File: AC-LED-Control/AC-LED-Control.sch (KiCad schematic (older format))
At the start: 20 parts, among them P101 CONN_01X02, P102 CONN_01X02, P103 CONN_01X04, SW101 SW_PUSH, U101 FOD814-D, U102 STM32F030F4P6, U103 74HC595, U104 74HC595

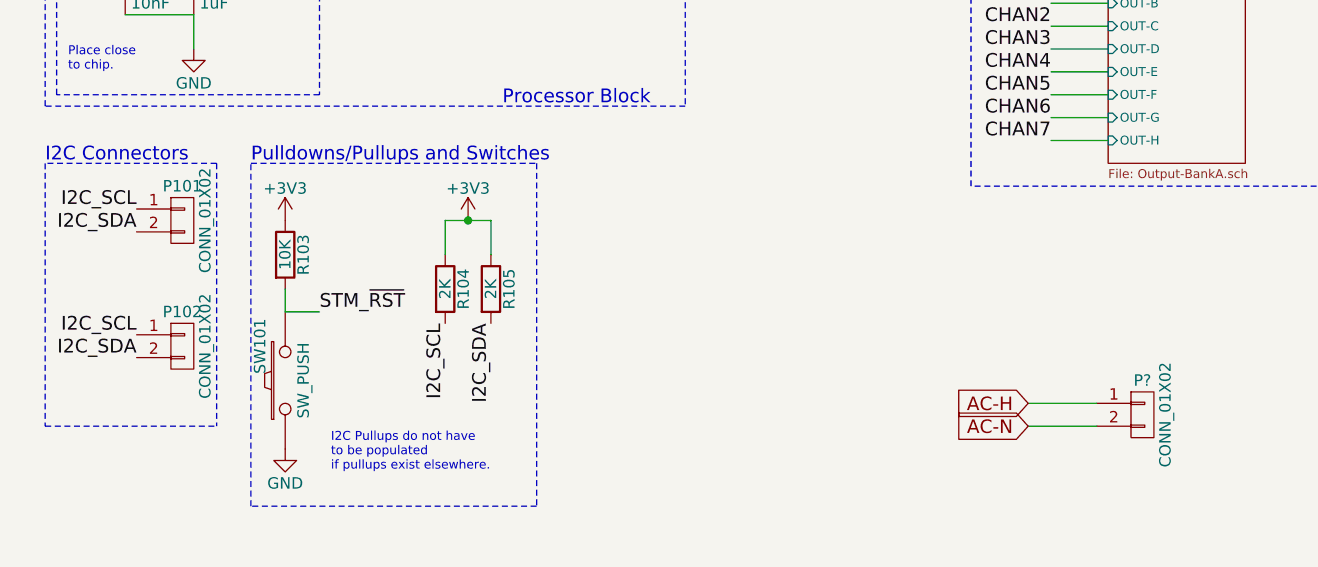
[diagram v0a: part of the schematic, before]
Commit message: Associated footprints
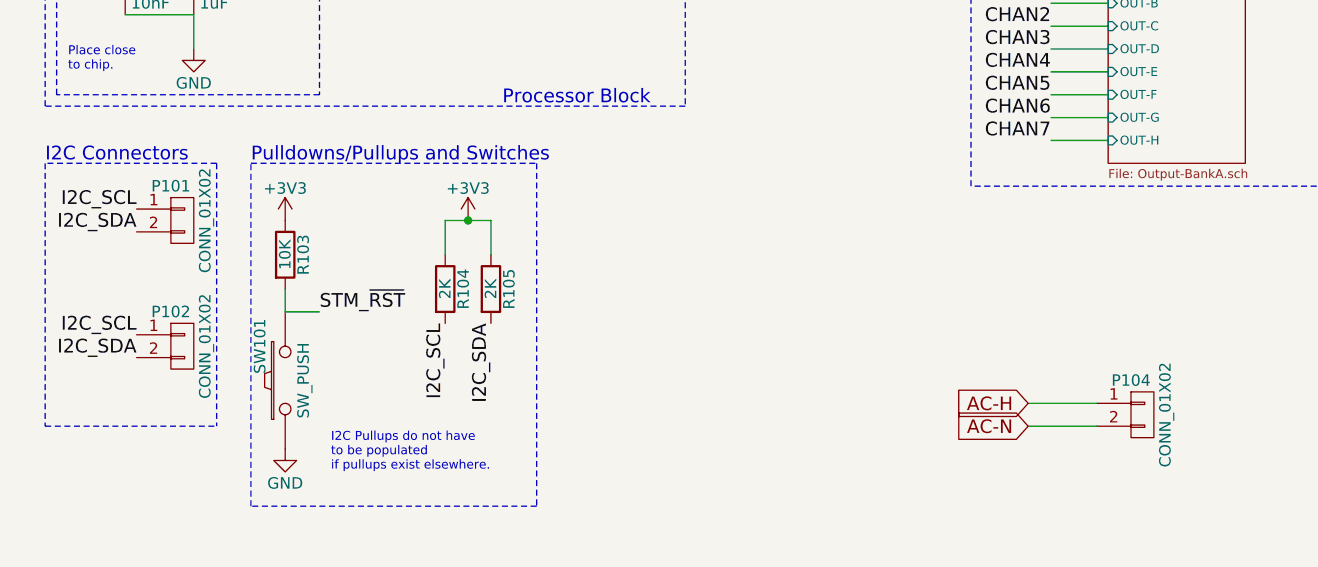
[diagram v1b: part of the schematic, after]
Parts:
- C101, C102, C103, C104, C105: footprint (none) -> Capacitors_SMD:C_0603_HandSoldering
- P101, P102: footprint (none) -> Pin_Headers:Pin_Header_Straight_1x02
- P103: footprint (none) -> Pin_Headers:Pin_Header_Straight_1x04
- R101, R102, R103, R104, R105, R106: footprint (none) -> Resistors_SMD:R_0603_HandSoldering
- SW101: footprint (none) -> Buttons_Switches_SMD:SW_SPST_EVPBF
- U101: footprint (none) -> onsemi:OnSemi_PDIP4
- U102: footprint (none) -> Housings_SSOP:TSSOP-20_4.4x6.5mm_Pitch0.65mm
- U103, U104: footprint (none) -> Housings_SOIC:SOIC-16_3.9x9.9mm_Pitch1.27mm
- gave numbers to parts that had none: 1
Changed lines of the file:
@@
 F 0 "U102" H 2200 700 60  0000 C CNN
 F 1 "STM32F030F4P6" H 2200 1950 60  0000 C CNN
-F 2 "" H 2150 1400 60  0000 C CNN
+F 2 "Housings_SSOP:TSSOP-20_4.4x6.5mm_Pitch0.65mm" H 2150 1400 60  0001 C CNN
 F 3 "" H 2150 1400 60  0000 C CNN
 	1    2200 1400
@@
 U 1 1 5B453C99
 P 1300 4350
-F 0 "P101" H 1300 4500 50  0000 C CNN
+F 0 "P101" H 1250 4500 50  0000 C CNN
 F 1 "CONN_01X02" V 1400 4350 50  0000 C CNN
-F 2 "" H 1300 4350 50  0000 C CNN
+F 2 "Pin_Headers:Pin_Header_Straight_1x02" H 1300 4350 50  0001 C CNN
 F 3 "" H 1300 4350 50  0000 C CNN
 	1    1300 4350
@@
 U 1 1 5B453DC6
 P 1300 4900
-F 0 "P102" H 1300 5050 50  0000 C CNN
+F 0 "P102" H 1250 5050 50  0000 C CNN
 F 1 "CONN_01X02" V 1400 4900 50  0000 C CNN
-F 2 "" H 1300 4900 50  0000 C CNN
+F 2 "Pin_Headers:Pin_Header_Straight_1x02" H 1300 4900 50  0001 C CNN
 F 3 "" H 1300 4900 50  0000 C CNN
 	1    1300 4900
@@
 F 0 "R104" V 2530 4650 50  0000 C CNN
 F 1 "2K" V 2450 4650 50  0000 C CNN
-F 2 "" V 2380 4650 50  0000 C CNN
+F 2 "Resistors_SMD:R_0603_HandSoldering" V 2380 4650 50  0001 C CNN
 F 3 "" H 2450 4650 50  0000 C CNN
 	1    2450 4650
@@
 F 0 "R105" V 2730 4650 50  0000 C CNN
 F 1 "2K" V 2650 4650 50  0000 C CNN
-F 2 "" V 2580 4650 50  0000 C CNN
+F 2 "Resistors_SMD:R_0603_HandSoldering" V 2580 4650 50  0001 C CNN
 F 3 "" H 2650 4650 50  0000 C CNN
 	1    2650 4650
@@
 $EndComp
 $Comp
-L +3V3 #PWR108
+L +3V3 #PWR01
 U 1 1 5B45401C
 P 2550 4350
-F 0 "#PWR108" H 2550 4200 50  0001 C CNN
+F 0 "#PWR01" H 2550 4200 50  0001 C CNN
 F 1 "+3V3" H 2550 4490 50  0000 C CNN
 F 2 "" H 2550 4350 50  0000 C CNN
@@
 F 0 "C101" H 1075 2750 50  0000 L CNN
 F 1 "100nF" H 1075 2550 50  0000 L CNN
-F 2 "" H 1088 2500 50  0000 C CNN
+F 2 "Capacitors_SMD:C_0603_HandSoldering" H 1088 2500 50  0001 C CNN
 F 3 "" H 1050 2650 50  0000 C CNN
 	1    1050 2650
@@
 F 0 "C103" H 1375 2750 50  0000 L CNN
 F 1 "100nF" H 1375 2550 50  0000 L CNN
-F 2 "" H 1388 2500 50  0000 C CNN
+F 2 "Capacitors_SMD:C_0603_HandSoldering" H 1388 2500 50  0001 C CNN
 F 3 "" H 1350 2650 50  0000 C CNN
 	1    1350 2650
@@
 F 0 "C105" H 1675 2750 50  0000 L CNN
 F 1 "4.7uF" H 1675 2550 50  0000 L CNN
-F 2 "" H 1688 2500 50  0000 C CNN
+F 2 "Capacitors_SMD:C_0603_HandSoldering" H 1688 2500 50  0001 C CNN
 F 3 "" H 1650 2650 50  0000 C CNN
 	1    1650 2650
@@
 	1400 1750 1400 1850
 $Comp
-L GND #PWR104
+L GND #PWR02
 U 1 1 5B454DB5
 P 1400 1850
-F 0 "#PWR104" H 1400 1600 50  0001 C CNN
+F 0 "#PWR02" H 1400 1600 50  0001 C CNN
 F 1 "GND" H 1400 1700 50  0000 C CNN
 F 2 "" H 1400 1850 50  0000 C CNN
@@
 $EndComp
 $Comp
-L GND #PWR105
+L GND #PWR03
 U 1 1 5B454DF7
 P 1650 2900
-F 0 "#PWR105" H 1650 2650 50  0001 C CNN
+F 0 "#PWR03" H 1650 2650 50  0001 C CNN
 F 1 "GND" H 1650 2750 50  0000 C CNN
 F 2 "" H 1650 2900 50  0000 C CNN
@@
 F 0 "C102" H 1075 3400 50  0000 L CNN
 F 1 "10nF" H 1075 3200 50  0000 L CNN
-F 2 "" H 1088 3150 50  0000 C CNN
+F 2 "Capacitors_SMD:C_0603_HandSoldering" H 1088 3150 50  0001 C CNN
 F 3 "" H 1050 3300 50  0000 C CNN
 	1    1050 3300
@@
 F 0 "C104" H 1375 3400 50  0000 L CNN
 F 1 "1uF" H 1375 3200 50  0000 L CNN
-F 2 "" H 1388 3150 50  0000 C CNN
+F 2 "Capacitors_SMD:C_0603_HandSoldering" H 1388 3150 50  0001 C CNN
 F 3 "" H 1350 3300 50  0000 C CNN
 	1    1350 3300
@@
 $EndComp
 $Comp
-L GND #PWR103
+L GND #PWR04
 U 1 1 5B454F8F
 P 1350 3600
-F 0 "#PWR103" H 1350 3350 50  0001 C CNN
+F 0 "#PWR04" H 1350 3350 50  0001 C CNN
 F 1 "GND" H 1350 3450 50  0000 C CNN
 F 2 "" H 1350 3600 50  0000 C CNN
@@
 F 0 "U104" H 8750 2550 50  0000 C CNN
 F 1 "74HC595" H 8600 1350 50  0000 C CNN
-F 2 "" H 8600 1950 50  0000 C CNN
+F 2 "Housings_SOIC:SOIC-16_3.9x9.9mm_Pitch1.27mm" H 8600 1950 50  0001 C CNN
 F 3 "" H 8600 1950 50  0000 C CNN
 	1    8600 1950
@@
 F 0 "U103" H 6150 2550 50  0000 C CNN
 F 1 "74HC595" H 6000 1350 50  0000 C CNN
-F 2 "" H 6000 1950 50  0000 C CNN
+F 2 "Housings_SOIC:SOIC-16_3.9x9.9mm_Pitch1.27mm" H 6000 1950 50  0001 C CNN
 F 3 "" H 6000 1950 50  0000 C CNN
 	1    6000 1950
@@
 	8300 1400 8300 1250
 $Comp
-L +3V3 #PWR115
+L +3V3 #PWR05
 U 1 1 5B455E79
 P 8300 1250
-F 0 "#PWR115" H 8300 1100 50  0001 C CNN
+F 0 "#PWR05" H 8300 1100 50  0001 C CNN
 F 1 "+3V3" H 8300 1390 50  0000 C CNN
 F 2 "" H 8300 1250 50  0000 C CNN
@@
 	8300 2500 8300 2650
 $Comp
-L GND #PWR116
+L GND #PWR06
 U 1 1 5B455F67
 P 8300 2650
-F 0 "#PWR116" H 8300 2400 50  0001 C CNN
+F 0 "#PWR06" H 8300 2400 50  0001 C CNN
 F 1 "GND" H 8300 2500 50  0000 C CNN
 F 2 "" H 8300 2650 50  0000 C CNN
@@
 	5700 1400 5700 1250
 $Comp
-L +3V3 #PWR113
+L +3V3 #PWR07
 U 1 1 5B456028
 P 5700 1250
-F 0 "#PWR113" H 5700 1100 50  0001 C CNN
+F 0 "#PWR07" H 5700 1100 50  0001 C CNN
 F 1 "+3V3" H 5700 1390 50  0000 C CNN
 F 2 "" H 5700 1250 50  0000 C CNN
@@
 	5700 2500 5700 2650
 $Comp
-L GND #PWR114
+L GND #PWR08
 U 1 1 5B4560F7
 P 5700 2650
-F 0 "#PWR114" H 5700 2400 50  0001 C CNN
+F 0 "#PWR08" H 5700 2400 50  0001 C CNN
 F 1 "GND" H 5700 2500 50  0000 C CNN
 F 2 "" H 5700 2650 50  0000 C CNN
@@
 	1750 4750 1750 4650
 $Comp
-L +3V3 #PWR106
+L +3V3 #PWR09
 U 1 1 5B4571F5
 P 1750 4350
-F 0 "#PWR106" H 1750 4200 50  0001 C CNN
+F 0 "#PWR09" H 1750 4200 50  0001 C CNN
 F 1 "+3V3" H 1750 4490 50  0000 C CNN
 F 2 "" H 1750 4350 50  0000 C CNN
@@
 F 0 "R103" V 1830 4500 50  0000 C CNN
 F 1 "10K" V 1750 4500 50  0000 C CNN
-F 2 "" V 1680 4500 50  0000 C CNN
+F 2 "Resistors_SMD:R_0603_HandSoldering" V 1680 4500 50  0001 C CNN
 F 3 "" H 1750 4500 50  0000 C CNN
 	1    1750 4500
@@
 F 0 "SW101" H 1900 5160 50  0000 C CNN
 F 1 "SW_PUSH" H 1750 4970 50  0000 C CNN
-F 2 "" H 1750 5050 50  0000 C CNN
+F 2 "Buttons_Switches_SMD:SW_SPST_EVPBF" H 1750 5050 50  0001 C CNN
 F 3 "" H 1750 5050 50  0000 C CNN
 	1    1750 5050
@@
 $EndComp
 $Comp
-L GND #PWR107
+L GND #PWR010
 U 1 1 5B4575F8
 P 1750 5350
-F 0 "#PWR107" H 1750 5100 50  0001 C CNN
+F 0 "#PWR010" H 1750 5100 50  0001 C CNN
 F 1 "GND" H 1750 5200 50  0000 C CNN
 F 2 "" H 1750 5350 50  0000 C CNN
@@
 	800  1000 800  1250
 $Comp
-L GND #PWR101
+L GND #PWR011
 U 1 1 5B45876A
 P 800 1250
-F 0 "#PWR101" H 800 1000 50  0001 C CNN
+F 0 "#PWR011" H 800 1000 50  0001 C CNN
 F 1 "GND" H 800 1100 50  0000 C CNN
 F 2 "" H 800 1250 50  0000 C CNN
@@
 F 0 "P103" H 2450 2500 50  0000 C CNN
 F 1 "CONN_01X04" V 2550 2750 50  0000 C CNN
-F 2 "" H 2450 2750 50  0000 C CNN
+F 2 "Pin_Headers:Pin_Header_Straight_1x04" H 2450 2750 50  0001 C CNN
 F 3 "" H 2450 2750 50  0000 C CNN
 	1    2450 2750
@@
 	3300 2800 3300 2700
 $Comp
-L +3V3 #PWR112
+L +3V3 #PWR012
 U 1 1 5B4593A7
 P 3300 2700
-F 0 "#PWR112" H 3300 2550 50  0001 C CNN
+F 0 "#PWR012" H 3300 2550 50  0001 C CNN
 F 1 "+3V3" H 3300 2840 50  0000 C CNN
 F 2 "" H 3300 2700 50  0000 C CNN
@@
 	2900 2900 2900 3000
 $Comp
-L GND #PWR111
+L GND #PWR013
 U 1 1 5B459412
 P 2900 3000
-F 0 "#PWR111" H 2900 2750 50  0001 C CNN
+F 0 "#PWR013" H 2900 2750 50  0001 C CNN
 F 1 "GND" H 2900 2850 50  0000 C CNN
 F 2 "" H 2900 3000 50  0000 C CNN
@@
 F 0 "R101" V 1580 6800 50  0000 C CNN
 F 1 "16K" V 1500 6800 50  0000 C CNN
-F 2 "" V 1430 6800 50  0000 C CNN
+F 2 "Resistors_SMD:R_0603_HandSoldering" V 1430 6800 50  0001 C CNN
 F 3 "" H 1500 6800 50  0000 C CNN
 	1    1500 6800
@@
 F 0 "U101" H 2050 6850 60  0000 C CNN
 F 1 "FOD814-D" H 2000 7550 60  0000 C CNN
-F 2 "" H 2000 7100 60  0000 C CNN
+F 2 "onsemi:OnSemi_PDIP4" H 2000 7100 60  0001 C CNN
 F 3 "" H 2000 7100 60  0000 C CNN
 	1    2050 7100
@@
 F 0 "R102" V 1580 7200 50  0000 C CNN
 F 1 "16K" V 1500 7200 50  0000 C CNN
-F 2 "" V 1430 7200 50  0000 C CNN
+F 2 "Resistors_SMD:R_0603_HandSoldering" V 1430 7200 50  0001 C CNN
 F 3 "" H 1500 7200 50  0000 C CNN
 	1    1500 7200
@@
 F 0 "R106" V 2730 6650 50  0000 C CNN
 F 1 "2K" V 2650 6650 50  0000 C CNN
-F 2 "" V 2580 6650 50  0000 C CNN
+F 2 "Resistors_SMD:R_0603_HandSoldering" V 2580 6650 50  0001 C CNN
 F 3 "" H 2650 6650 50  0000 C CNN
 	1    2650 6650
@@
 $EndComp
 $Comp
-L +3V3 #PWR109
+L +3V3 #PWR014
 U 1 1 5B463D3E
 P 2650 6500
-F 0 "#PWR109" H 2650 6350 50  0001 C CNN
+F 0 "#PWR014" H 2650 6350 50  0001 C CNN
 F 1 "+3V3" H 2650 6640 50  0000 C CNN
 F 2 "" H 2650 6500 50  0000 C CNN
@@
 	2650 7200 2650 7300
 $Comp
-L GND #PWR110
+L GND #PWR015
 U 1 1 5B464157
 P 2650 7300
-F 0 "#PWR110" H 2650 7050 50  0001 C CNN
+F 0 "#PWR015" H 2650 7050 50  0001 C CNN
 F 1 "GND" H 2650 7150 50  0000 C CNN
 F 2 "" H 2650 7300 50  0000 C CNN
@@
 Connection ~ 1150 1650
 $Comp
-L +3V3 #PWR102
+L +3V3 #PWR016
 U 1 1 5B465D50
 P 950 1650
-F 0 "#PWR102" H 950 1500 50  0001 C CNN
+F 0 "#PWR016" H 950 1500 50  0001 C CNN
 F 1 "+3V3" H 950 1790 50  0000 C CNN
 F 2 "" H 950 1650 50  0000 C CNN
@@
 	650  7500 650  6300
 $Comp
-L CONN_01X02 P?
+L CONN_01X02 P104
 U 1 1 5B47C991
 P 5500 5200
-F 0 "P?" H 5500 5350 50  0000 C CNN
+F 0 "P104" H 5450 5350 50  0000 C CNN
 F 1 "CONN_01X02" V 5600 5200 50  0000 C CNN
-F 2 "" H 5500 5200 50  0000 C CNN
+F 2 "" H 5500 5200 50  0001 C CNN
 F 3 "" H 5500 5200 50  0000 C CNN
 	1    5500 5200

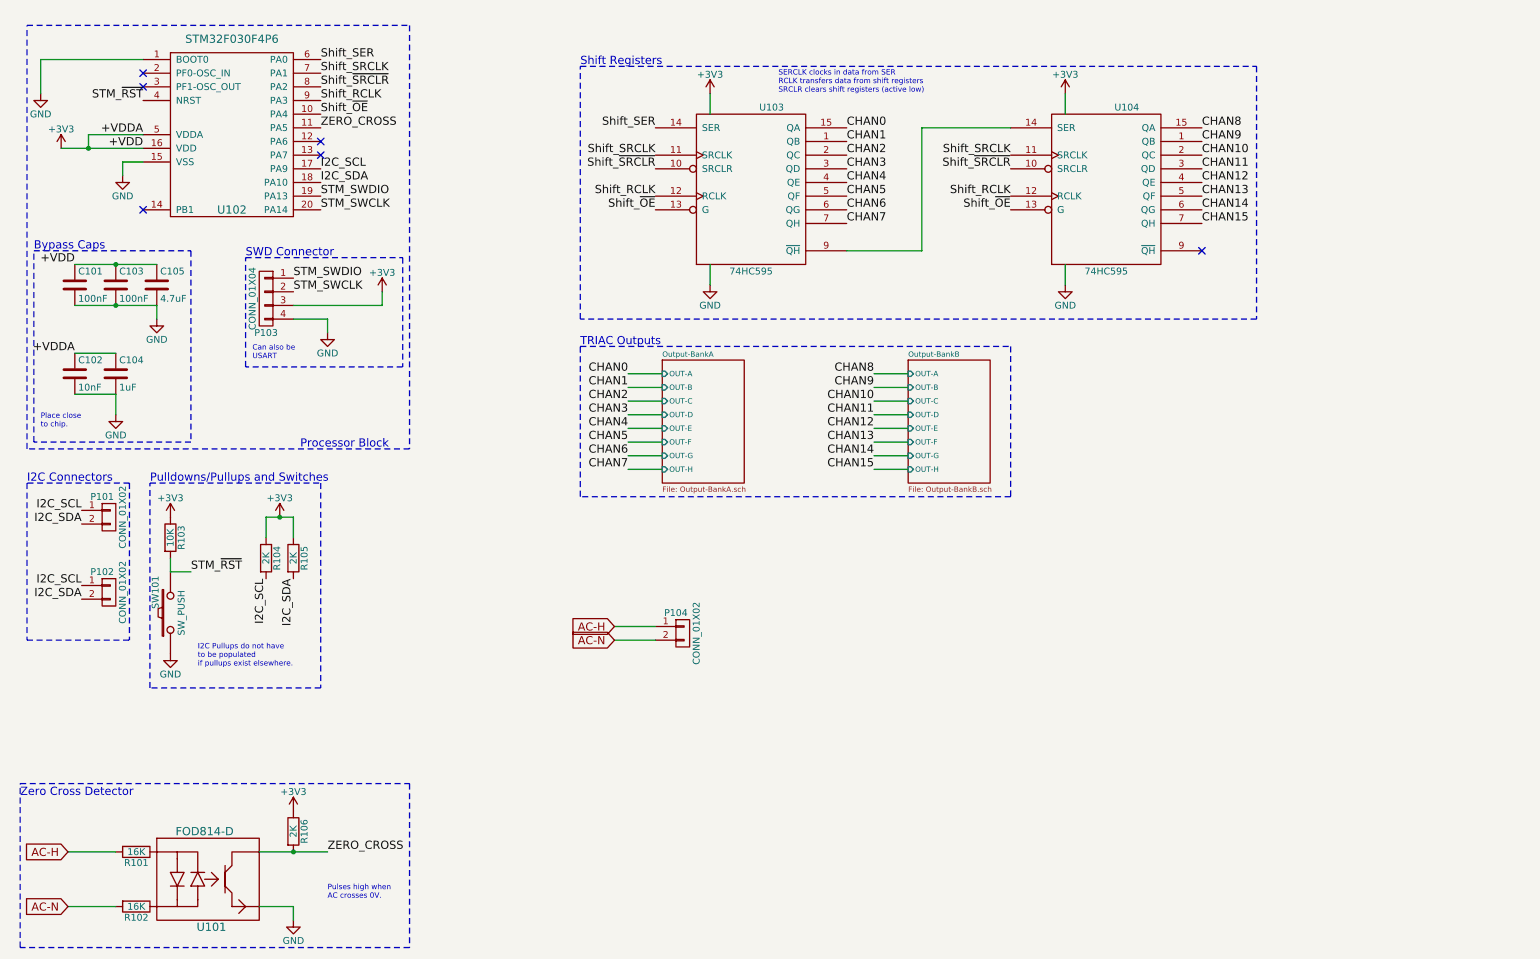
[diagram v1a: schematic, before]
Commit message: Added indication LEDs, 3v3 current specs and some initial layout
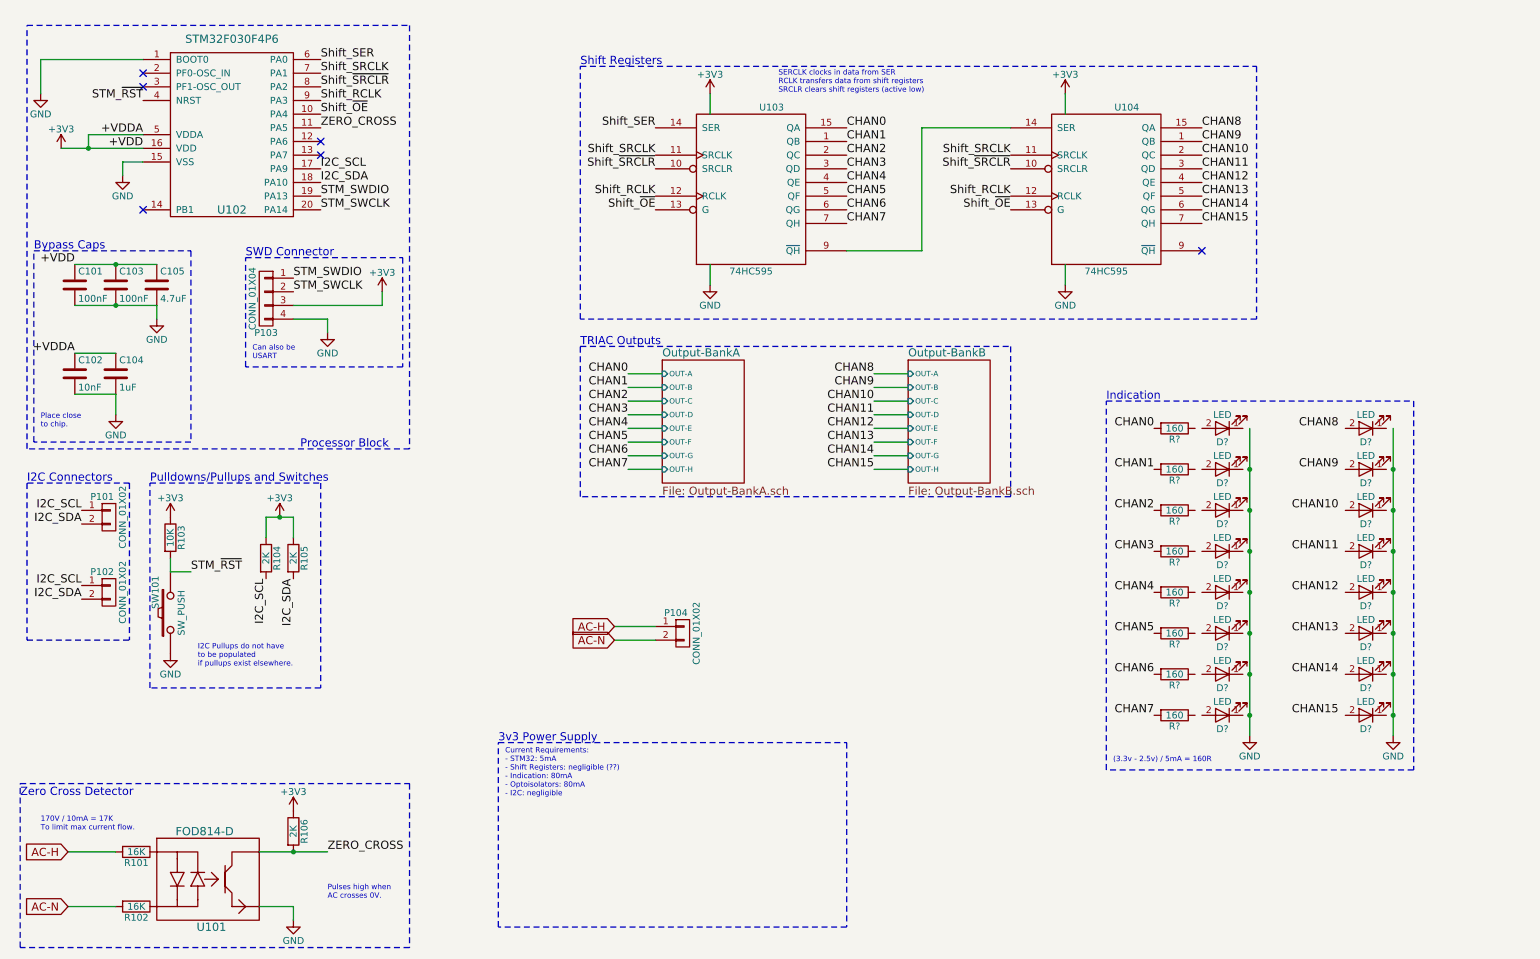
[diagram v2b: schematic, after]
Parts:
- added D? (x16): LED, symbol LED
- added R? (x8): 160, symbol R
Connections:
- wire segments 52 -> 54
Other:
- note added: "(3.3v - 2.5v) / 5mA = 160R"
- note added: "170V / 10mA = 17K\nTo limit max current flow."
- note added: "3v3 Power Supply\n"
- note added: "Current Requirements:\n- STM32: 5mA\n- Shift Registers: negligible (??)\n- Indication: 80mA\n- Optoisolators: 80mA\n- I2C: negligible"
- note added: "Indication"
